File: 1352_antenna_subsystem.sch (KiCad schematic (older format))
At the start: 26 parts, among them U1 cc1352p

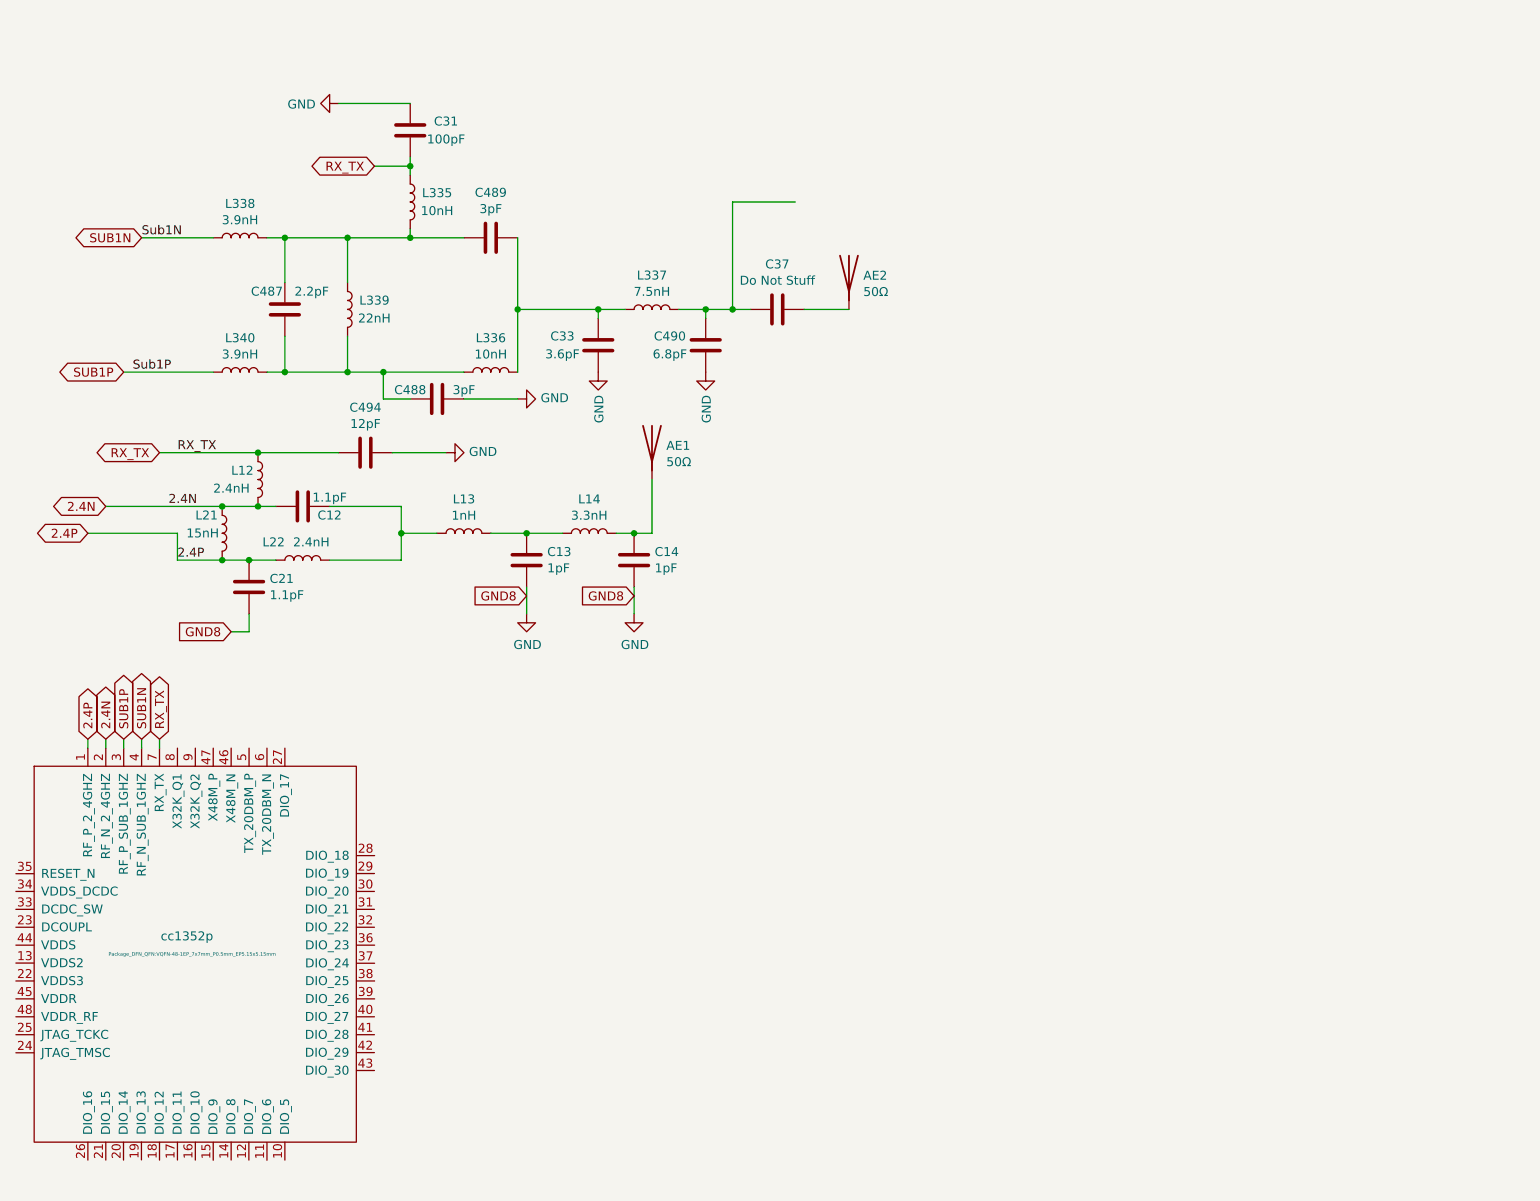
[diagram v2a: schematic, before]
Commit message: Added new symbols and footprints | Updated schematic for RF
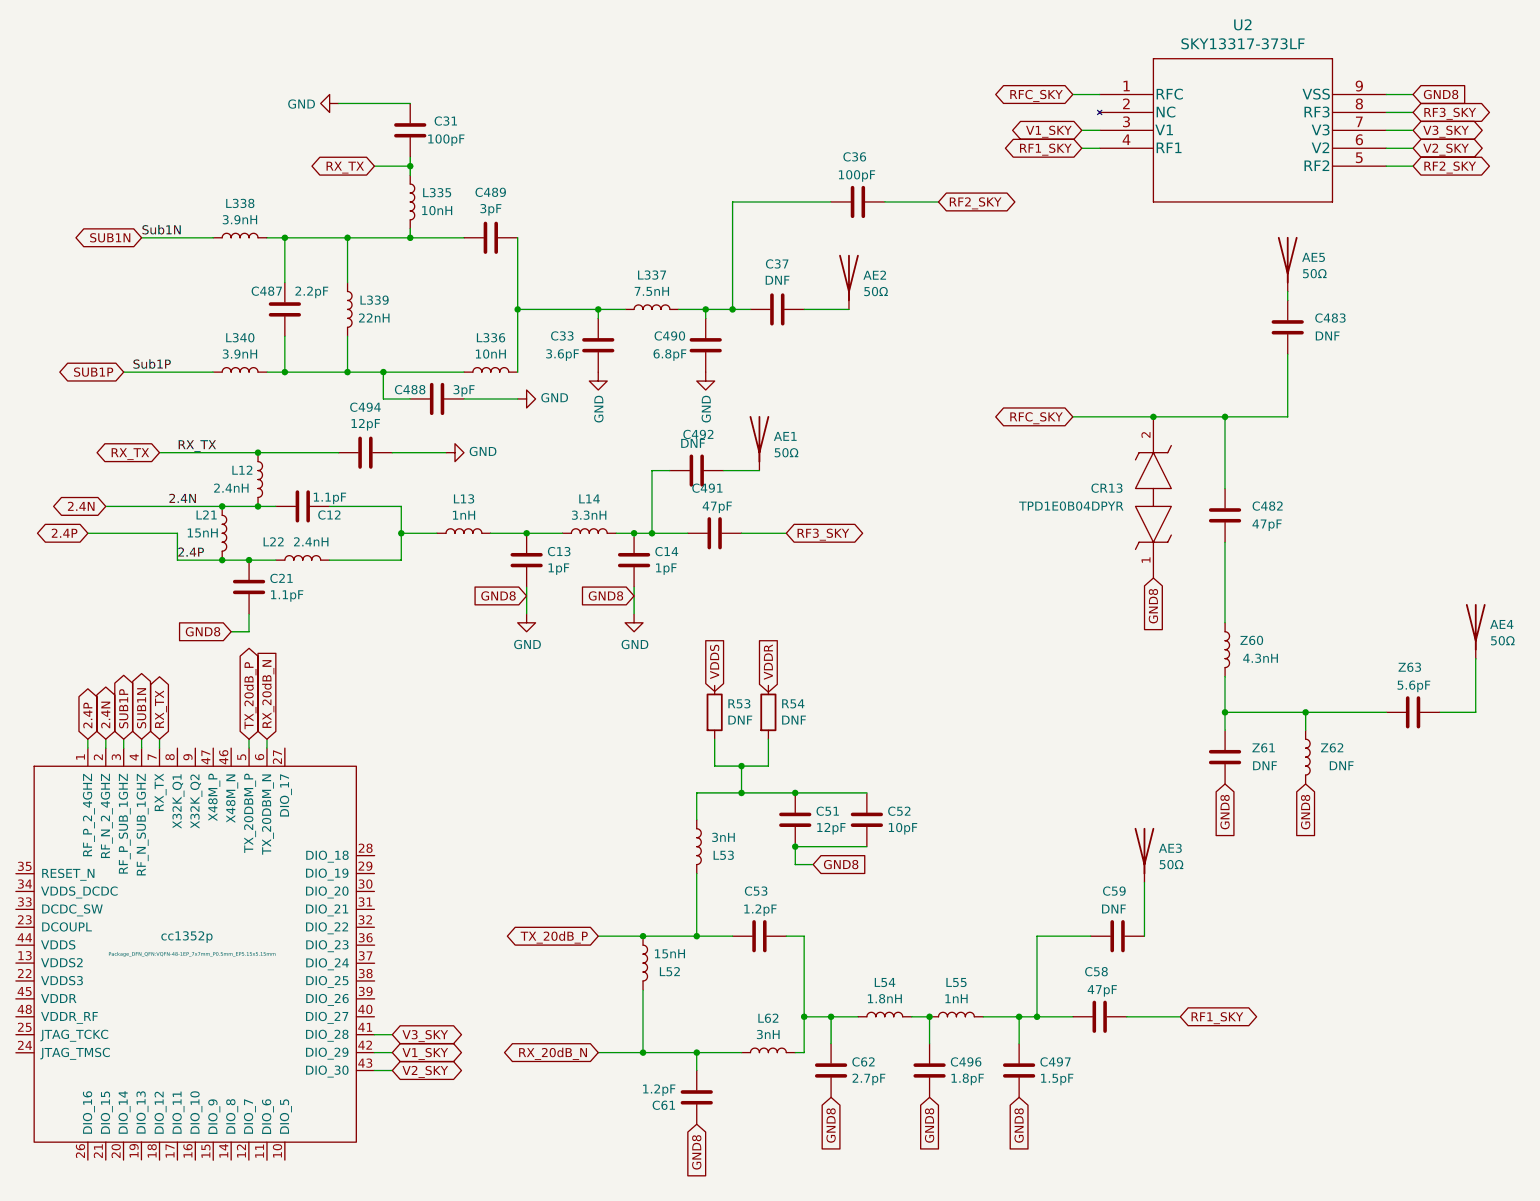
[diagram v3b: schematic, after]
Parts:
- added AE3, AE4, AE5: 50Ω, Connector_Coaxial:U.FL_Hirose_U.FL-R-SMT-1_Vertical, symbol Device:Antenna
- added C36: 100pF, Capacitor_SMD:C_0805_2012Metric_Pad1.18x1.45mm_HandSolder, symbol Device:C
- added C482, C491, C58: 47pF, Capacitor_SMD:C_0805_2012Metric_Pad1.18x1.45mm_HandSolder, symbol Device:C
- added C483, C492, C59, Z61: DNF, Capacitor_SMD:C_0805_2012Metric_Pad1.18x1.45mm_HandSolder, symbol Device:C
- added C496: 1.8pF, Capacitor_SMD:C_0805_2012Metric_Pad1.18x1.45mm_HandSolder, symbol Device:C
- added C497: 1.5pF, Capacitor_SMD:C_0805_2012Metric_Pad1.18x1.45mm_HandSolder, symbol Device:C
- added C51: 12pF, Capacitor_SMD:C_0805_2012Metric_Pad1.18x1.45mm_HandSolder, symbol Device:C
- added C52: 10pF, Capacitor_SMD:C_0805_2012Metric_Pad1.18x1.45mm_HandSolder, symbol Device:C
- added C53, C61: 1.2pF, Capacitor_SMD:C_0805_2012Metric_Pad1.18x1.45mm_HandSolder, symbol Device:C
- added C62: 2.7pF, Capacitor_SMD:C_0805_2012Metric_Pad1.18x1.45mm_HandSolder, symbol Device:C
- added CR13: TPD1E0B04DPYR, TPD1E0B04DPYR, symbol SamacSys_Parts:TPD1E0B04DPYR
- added L52: 15nH, Inductor_SMD:L_0805_2012Metric_Pad1.15x1.40mm_HandSolder, symbol Device:L
- added L53, L62: 3nH, Inductor_SMD:L_0805_2012Metric_Pad1.15x1.40mm_HandSolder, symbol Device:L
- added L54: 1.8nH, Inductor_SMD:L_0805_2012Metric_Pad1.15x1.40mm_HandSolder, symbol Device:L
- added L55: 1nH, Inductor_SMD:L_0805_2012Metric_Pad1.15x1.40mm_HandSolder, symbol Device:L
- added R53, R54: DNF, symbol Device:R
- added U2: SKY13317-373LF, MLP8_1P5X1P5_SKY, symbol SKY13317-373:SKY13317-373LF
- added Z60: 4.3nH, Inductor_SMD:L_0805_2012Metric_Pad1.15x1.40mm_HandSolder, symbol Device:L
- added Z62: DNF, Inductor_SMD:L_0805_2012Metric_Pad1.15x1.40mm_HandSolder, symbol Device:L
- added Z63: 5.6pF, Capacitor_SMD:C_0805_2012Metric_Pad1.18x1.45mm_HandSolder, symbol Device:C
- C37: value Do Not Stuff -> DNF
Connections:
- net GND: now also C496.2, C497.2, C51.2, C52.2, C61.1, C62.2, CR13.1, U2.9 (VSS), Z61.2, Z62.2
- net at C14.1, L14.2: now also C491.1, C492.1; no longer AE1.1 (A)
- net V3_SKY: now reaches U1.41 (DIO_28)
- net V3_SKY: now also U2.7 (V3)
- net V1_SKY: now reaches U1.42 (DIO_29)
- net V1_SKY: now also U2.3 (V1)
- net V2_SKY: now reaches U1.43 (DIO_30)
- net V2_SKY: now also U2.6 (V2)
- net TX_20dB_P: now reaches U1.5 (TX_20DBM_P)
- net TX_20dB_P: now also C53.1, L52.1, L53.2
- net RX_20dB_N: now reaches U1.6 (TX_20DBM_N)
- net RX_20dB_N: now also C61.2, L52.2, L62.1
- net at C37.2, C490.1, L337.2: now also C36.1
- new net: AE1.1 (A), C492.2
- new net: C53.2, C62.1, L54.1, L62.2
- new net: C51.1, C52.1, L53.1, R53.2, R54.2
- new net: C496.1, L54.2, L55.1
- new net: C497.1, C58.1, C59.1, L55.2
- new net: AE3.1 (A), C59.2
- new net: C482.2, Z60.1
- new net: Z60.2, Z61.1, Z62.1, Z63.1
- new net: AE4.1 (A), Z63.2
- new net: AE5.1 (A), C483.1
- new net RF1_SKY: C58.2, U2.4 (RF1)
- new net RF2_SKY: C36.2, U2.5 (RF2)
- new net RF3_SKY: C491.2, U2.8 (RF3)
- new net RFC_SKY: C482.1, C483.2, CR13.2, U2.1 (RFC)
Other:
- moved on the sheet: AE1

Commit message: Part way through rats nest of 20dB branch and RF switcher
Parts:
- removed U2: SKY13317-373LF, MLP8_1P5X1P5_SKY, symbol SKY13317-373:SKY13317-373LF
- added U2: SKY13317-373LF, footprints:SKY13317-373LF, symbol 2021-04-02_19-11-57:SKY13317-373LF
- R53, R54: footprint (none) -> Resistor_SMD:R_0805_2012Metric_Pad1.20x1.40mm_HandSolder
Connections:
- net GND: now also U2.9 (VSS)
- net RF1_SKY: now also U2.4 (RF1)
- net RF2_SKY: now also U2.5 (RF2)
- net RF3_SKY: now also U2.8 (RF3)
- net RFC_SKY: now also U2.1 (RFC)
- net V1_SKY: now also U2.3 (V1)
- net V2_SKY: now also U2.6 (V2)
- net V3_SKY: now also U2.7 (V3)
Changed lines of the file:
@@
 F 0 "R53" H 4920 4546 50  0000 L CNN
 F 1 "DNF" H 4920 4455 50  0000 L CNN
-F 2 "" V 4780 4500 50  0001 C CNN
+F 2 "Resistor_SMD:R_0805_2012Metric_Pad1.20x1.40mm_HandSolder" V 4780 4500 50  0001 C CNN
 F 3 "~" H 4850 4500 50  0001 C CNN
 	1    4850 4500
@@
 F 0 "R54" H 5220 4546 50  0000 L CNN
 F 1 "DNF" H 5220 4455 50  0000 L CNN
-F 2 "" V 5080 4500 50  0001 C CNN
+F 2 "Resistor_SMD:R_0805_2012Metric_Pad1.20x1.40mm_HandSolder" V 5080 4500 50  0001 C CNN
 F 3 "~" H 5150 4500 50  0001 C CNN
 	1    5150 4500
@@
 	0    -1   -1   0
 $EndComp
-$Comp
-L SKY13317-373:SKY13317-373LF U2
-U 1 1 6067B986
-P 7000 1050
-F 0 "U2" H 7800 1437 60  0000 C CNN
-F 1 "SKY13317-373LF" H 7800 1331 60  0000 C CNN
-F 2 "MLP8_1P5X1P5_SKY" H 7800 1290 60  0001 C CNN
-F 3 "" H 7000 1050 60  0000 C CNN
-	1    7000 1050
-	1    0    0    -1
-$EndComp
 Text GLabel 5250 3500 2    50   BiDi ~ 0
 RF3_SKY
@@
 Text GLabel 6850 1050 0    50   BiDi ~ 0
 RFC_SKY
-Wire Wire Line
-	6850 1050 7000 1050
 Text GLabel 6850 2850 0    50   BiDi ~ 0
 RFC_SKY
@@
 Wire Wire Line
 	4750 5400 4750 5750
+$Comp
+L 2021-04-02_19-11-57:SKY13317-373LF U2
+U 1 1 6068C4D3
+P 7000 1050
+F 0 "U2" H 7800 1437 60  0000 C CNN
+F 1 "SKY13317-373LF" H 7800 1331 60  0000 C CNN
+F 2 "footprints:SKY13317-373LF" H 7800 1290 60  0001 C CNN
+F 3 "" H 7000 1050 60  0000 C CNN
+	1    7000 1050
+	1    0    0    -1
+$EndComp
+Wire Wire Line
+	6850 1050 7000 1050
 $EndSCHEMATC

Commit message: Just a summer update to make sure we're all on the same page
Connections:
- net at Z63.2: no longer AE4.1 (A)
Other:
- moved on the sheet: L52, Z63
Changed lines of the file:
@@
 $Descr A4 11693 8268
 encoding utf-8
-Sheet 2 2
+Sheet 2 3
 Title ""
 Date ""
@@
 Wire Wire Line
 	2250 4700 2250 4650
-Text GLabel 2350 4650 1    50   Input ~ 0
+Text GLabel 2350 4650 1    50   BiDi ~ 0
 RX_20dB_N
-Wire Wire Line
-	2350 4700 2350 4650
 Text GLabel 4200 5750 0    50   BiDi ~ 0
 TX_20dB_P
@@
 L Device:L L52
 U 1 1 605D71FC
-P 4450 5900
-F 0 "L52" H 4600 5850 50  0000 C CNN
-F 1 "15nH" H 4600 5950 50  0000 C CNN
-F 2 "Inductor_SMD:L_0805_2012Metric_Pad1.15x1.40mm_HandSolder" H 4450 5900 50  0001 C CNN
-F 3 "~" H 4450 5900 50  0001 C CNN
-	1    4450 5900
-	1    0    0    -1
-$EndComp
-Wire Wire Line
-	4200 5750 4450 5750
-Wire Wire Line
-	4450 6400 4200 6400
-Wire Wire Line
-	4450 6050 4450 6400
-Wire Wire Line
-	4450 6400 4750 6400
-Connection ~ 4450 6400
+P 4450 6050
+F 0 "L52" H 4600 6000 50  0000 C CNN
+F 1 "15nH" H 4600 6100 50  0000 C CNN
+F 2 "Inductor_SMD:L_0805_2012Metric_Pad1.15x1.40mm_HandSolder" H 4450 6050 50  0001 C CNN
+F 3 "~" H 4450 6050 50  0001 C CNN
+	1    4450 6050
+	1    0    0    -1
+$EndComp
 Wire Wire Line
 	4750 6400 4750 6500
@@
 GND8
 Wire Wire Line
-	8150 4500 8600 4500
+	8150 4500 8550 4500
 $Comp
 L Device:C Z63
 U 1 1 6075DD50
-P 8750 4500
-F 0 "Z63" V 9000 4450 50  0000 L CNN
-F 1 "5.6pF" V 8900 4400 50  0000 L CNN
-F 2 "Capacitor_SMD:C_0805_2012Metric_Pad1.18x1.45mm_HandSolder" H 8788 4350 50  0001 C CNN
-F 3 "~" H 8750 4500 50  0001 C CNN
-	1    8750 4500
+P 8700 4500
+F 0 "Z63" V 8950 4450 50  0000 L CNN
+F 1 "5.6pF" V 8850 4400 50  0000 L CNN
+F 2 "Capacitor_SMD:C_0805_2012Metric_Pad1.18x1.45mm_HandSolder" H 8738 4350 50  0001 C CNN
+F 3 "~" H 8700 4500 50  0001 C CNN
+	1    8700 4500
 	0    -1   -1   0
 $EndComp
@@
 Wire Wire Line
 	4500 3150 4500 3500
-Connection ~ 4450 5750
 Wire Wire Line
 	5250 5750 5350 5750
 Wire Wire Line
 	5350 5750 5350 6200
-Wire Wire Line
-	4450 5750 4750 5750
 Connection ~ 4750 5750
 Wire Wire Line
@@
 Wire Wire Line
 	6850 1050 7000 1050
+Connection ~ 8550 4500
+Wire Wire Line
+	8550 4500 8600 4500
+Wire Wire Line
+	4200 5750 4450 5750
+Wire Wire Line
+	4200 6400 4450 6400
+Wire Wire Line
+	4450 5900 4450 5750
+Connection ~ 4450 5750
+Wire Wire Line
+	4450 5750 4750 5750
+Wire Wire Line
+	4450 6200 4450 6400
+Connection ~ 4450 6400
+Wire Wire Line
+	4450 6400 4750 6400
+Wire Wire Line
+	2350 4650 2350 4700
 $EndSCHEMATC
